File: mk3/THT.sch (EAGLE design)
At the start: 13 parts, among them IC1 74HC4053P

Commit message: Changed base resistor to 1k.
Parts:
- R3: value 330 -> 1K
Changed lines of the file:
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@@
 <grid distance="0.1" unitdist="inch" unit="inch" style="lines" multiple="1" display="no" altdistance="0.01" altunitdist="inch" altunit="inch"/>
 <layers>
-<layer number="1" name="Top" color="4" fill="1" visible="yes" active="no"/>
-<layer number="16" name="Bottom" color="1" fill="1" visible="yes" active="no"/>
-<layer number="17" name="Pads" color="2" fill="1" visible="yes" active="no"/>
-<layer number="18" name="Vias" color="2" fill="1" visible="yes" active="no"/>
-<layer number="19" name="Unrouted" color="6" fill="1" visible="yes" active="no"/>
-<layer number="20" name="Dimension" color="15" fill="1" visible="yes" active="no"/>
-<layer number="21" name="tPlace" color="7" fill="1" visible="yes" active="no"/>
-<layer number="22" name="bPlace" color="7" fill="1" visible="yes" active="no"/>
-<layer number="23" name="tOrigins" color="15" fill="1" visible="yes" active="no"/>
-<layer number="24" name="bOrigins" color="15" fill="1" visible="yes" active="no"/>
-<layer number="25" name="tNames" color="7" fill="1" visible="yes" active="no"/>
-<layer number="26" name="bNames" color="7" fill="1" visible="yes" active="no"/>
-<layer number="27" name="tValues" color="7" fill="1" visible="yes" active="no"/>
-<layer number="28" name="bValues" color="7" fill="1" visible="yes" active="no"/>
+<layer number="1" name="Top" color="4" fill="1" visible="no" active="no"/>
+<layer number="16" name="Bottom" color="1" fill="1" visible="no" active="no"/>
+<layer number="17" name="Pads" color="2" fill="1" visible="no" active="no"/>
+<layer number="18" name="Vias" color="2" fill="1" visible="no" active="no"/>
+<layer number="19" name="Unrouted" color="6" fill="1" visible="no" active="no"/>
+<layer number="20" name="Dimension" color="15" fill="1" visible="no" active="no"/>
+<layer number="21" name="tPlace" color="7" fill="1" visible="no" active="no"/>
+<layer number="22" name="bPlace" color="7" fill="1" visible="no" active="no"/>
+<layer number="23" name="tOrigins" color="15" fill="1" visible="no" active="no"/>
+<layer number="24" name="bOrigins" color="15" fill="1" visible="no" active="no"/>
+<layer number="25" name="tNames" color="7" fill="1" visible="no" active="no"/>
+<layer number="26" name="bNames" color="7" fill="1" visible="no" active="no"/>
+<layer number="27" name="tValues" color="7" fill="1" visible="no" active="no"/>
+<layer number="28" name="bValues" color="7" fill="1" visible="no" active="no"/>
 <layer number="29" name="tStop" color="7" fill="3" visible="no" active="no"/>
 <layer number="30" name="bStop" color="7" fill="6" visible="no" active="no"/>
@@
 <layer number="35" name="tGlue" color="7" fill="4" visible="no" active="no"/>
 <layer number="36" name="bGlue" color="7" fill="5" visible="no" active="no"/>
-<layer number="37" name="tTest" color="7" fill="1" visible="yes" active="no"/>
-<layer number="38" name="bTest" color="7" fill="1" visible="yes" active="no"/>
+<layer number="37" name="tTest" color="7" fill="1" visible="no" active="no"/>
+<layer number="38" name="bTest" color="7" fill="1" visible="no" active="no"/>
 <layer number="39" name="tKeepout" color="4" fill="11" visible="no" active="no"/>
 <layer number="40" name="bKeepout" color="1" fill="11" visible="no" active="no"/>
@@
 <layer number="44" name="Drills" color="7" fill="1" visible="no" active="no"/>
 <layer number="45" name="Holes" color="7" fill="1" visible="no" active="no"/>
-<layer number="46" name="Milling" color="3" fill="1" visible="yes" active="no"/>
-<layer number="47" name="Measures" color="7" fill="1" visible="yes" active="no"/>
-<layer number="48" name="Document" color="7" fill="1" visible="yes" active="no"/>
-<layer number="49" name="Reference" color="7" fill="1" visible="yes" active="no"/>
-<layer number="50" name="dxf" color="7" fill="1" visible="yes" active="no"/>
-<layer number="51" name="tDocu" color="7" fill="1" visible="yes" active="no"/>
-<layer number="52" name="bDocu" color="7" fill="1" visible="yes" active="no"/>
-<layer number="53" name="tGND_GNDA" color="7" fill="9" visible="yes" active="no"/>
-<layer number="54" name="bGND_GNDA" color="1" fill="9" visible="yes" active="no"/>
-<layer number="56" name="wert" color="7" fill="1" visible="yes" active="no"/>
-<layer number="57" name="tCAD" color="7" fill="1" visible="yes" active="no"/>
-<layer number="59" name="tCarbon" color="7" fill="1" visible="yes" active="no"/>
-<layer number="60" name="bCarbon" color="7" fill="1" visible="yes" active="no"/>
+<layer number="46" name="Milling" color="3" fill="1" visible="no" active="no"/>
+<layer number="47" name="Measures" color="7" fill="1" visible="no" active="no"/>
+<layer number="48" name="Document" color="7" fill="1" visible="no" active="no"/>
+<layer number="49" name="Reference" color="7" fill="1" visible="no" active="no"/>
+<layer number="50" name="dxf" color="7" fill="1" visible="no" active="no"/>
+<layer number="51" name="tDocu" color="7" fill="1" visible="no" active="no"/>
+<layer number="52" name="bDocu" color="7" fill="1" visible="no" active="no"/>
+<layer number="53" name="tGND_GNDA" color="7" fill="9" visible="no" active="no"/>
+<layer number="54" name="bGND_GNDA" color="1" fill="9" visible="no" active="no"/>
+<layer number="56" name="wert" color="7" fill="1" visible="no" active="no"/>
+<layer number="57" name="tCAD" color="7" fill="1" visible="no" active="no"/>
+<layer number="59" name="tCarbon" color="7" fill="1" visible="no" active="no"/>
+<layer number="60" name="bCarbon" color="7" fill="1" visible="no" active="no"/>
 <layer number="90" name="Modules" color="5" fill="1" visible="yes" active="yes"/>
 <layer number="91" name="Nets" color="2" fill="1" visible="yes" active="yes"/>
@@
 <part name="T1" library="transistor-neu-to92" deviceset="*-NPN-" device="TO92-EBC" technology="2N3904"/>
 <part name="P+2" library="supply1" deviceset="VCC" device=""/>
-<part name="R3" library="rcl" deviceset="R-EU_" device="0207/2V" value="330"/>
+<part name="R3" library="rcl" deviceset="R-EU_" device="0207/2V" value="1K"/>
 <part name="GND3" library="supply1" deviceset="GND" device=""/>
 <part name="JP2" library="jumper" deviceset="JP2E" device=""/>

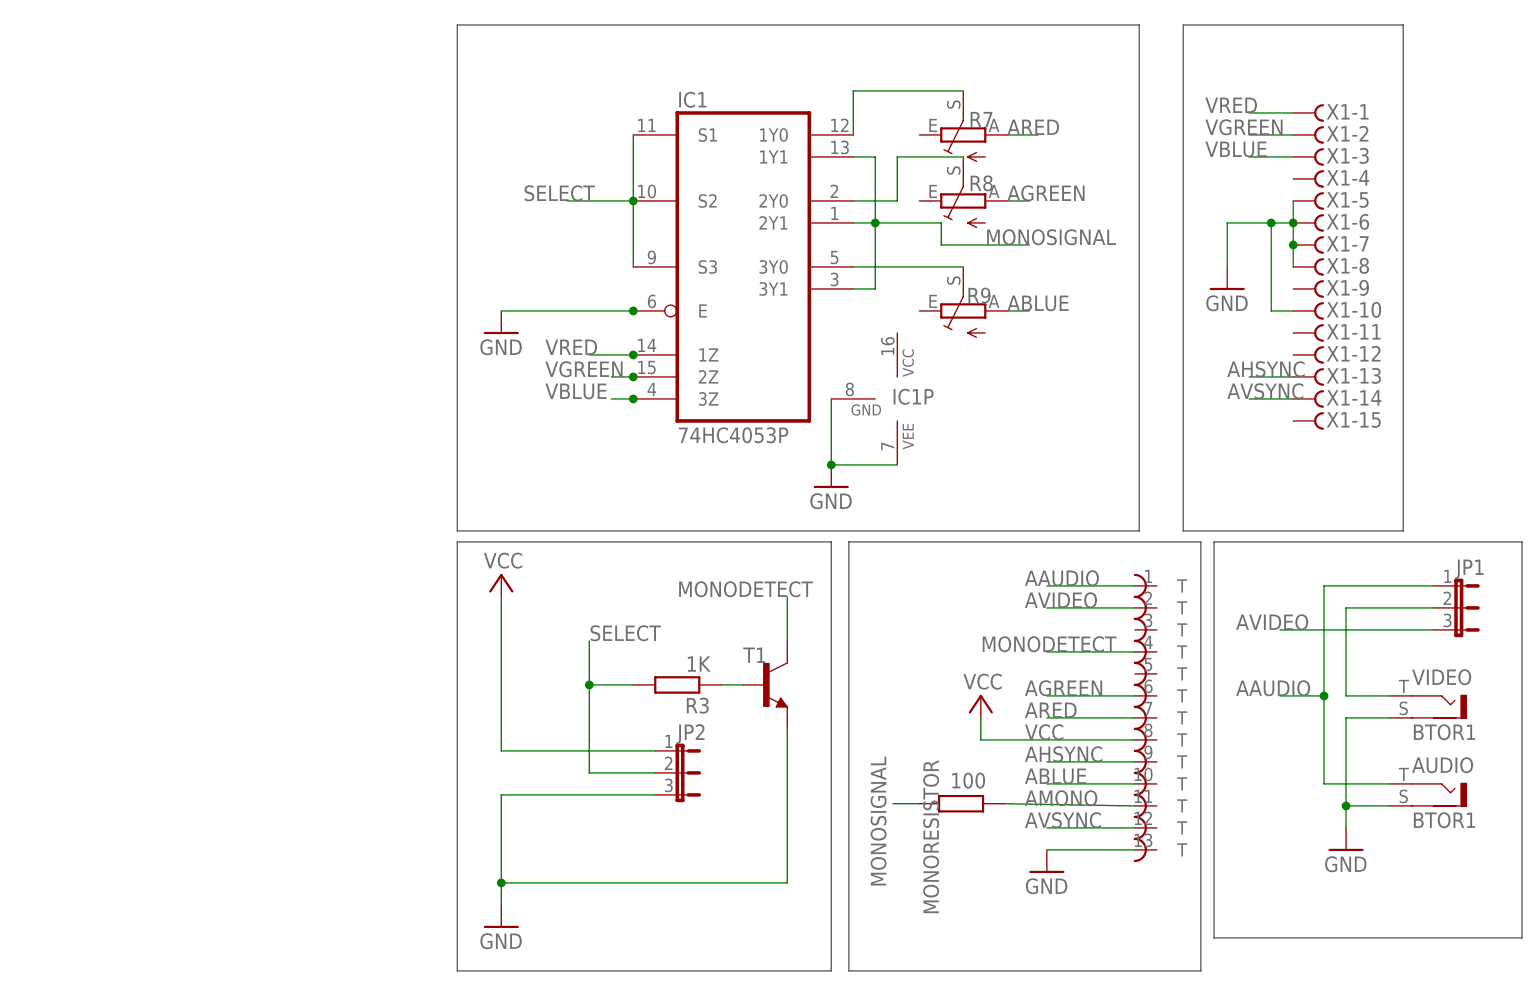
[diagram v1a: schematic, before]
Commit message: Switched to CD4053, didn't check the ratings on the HC-one.
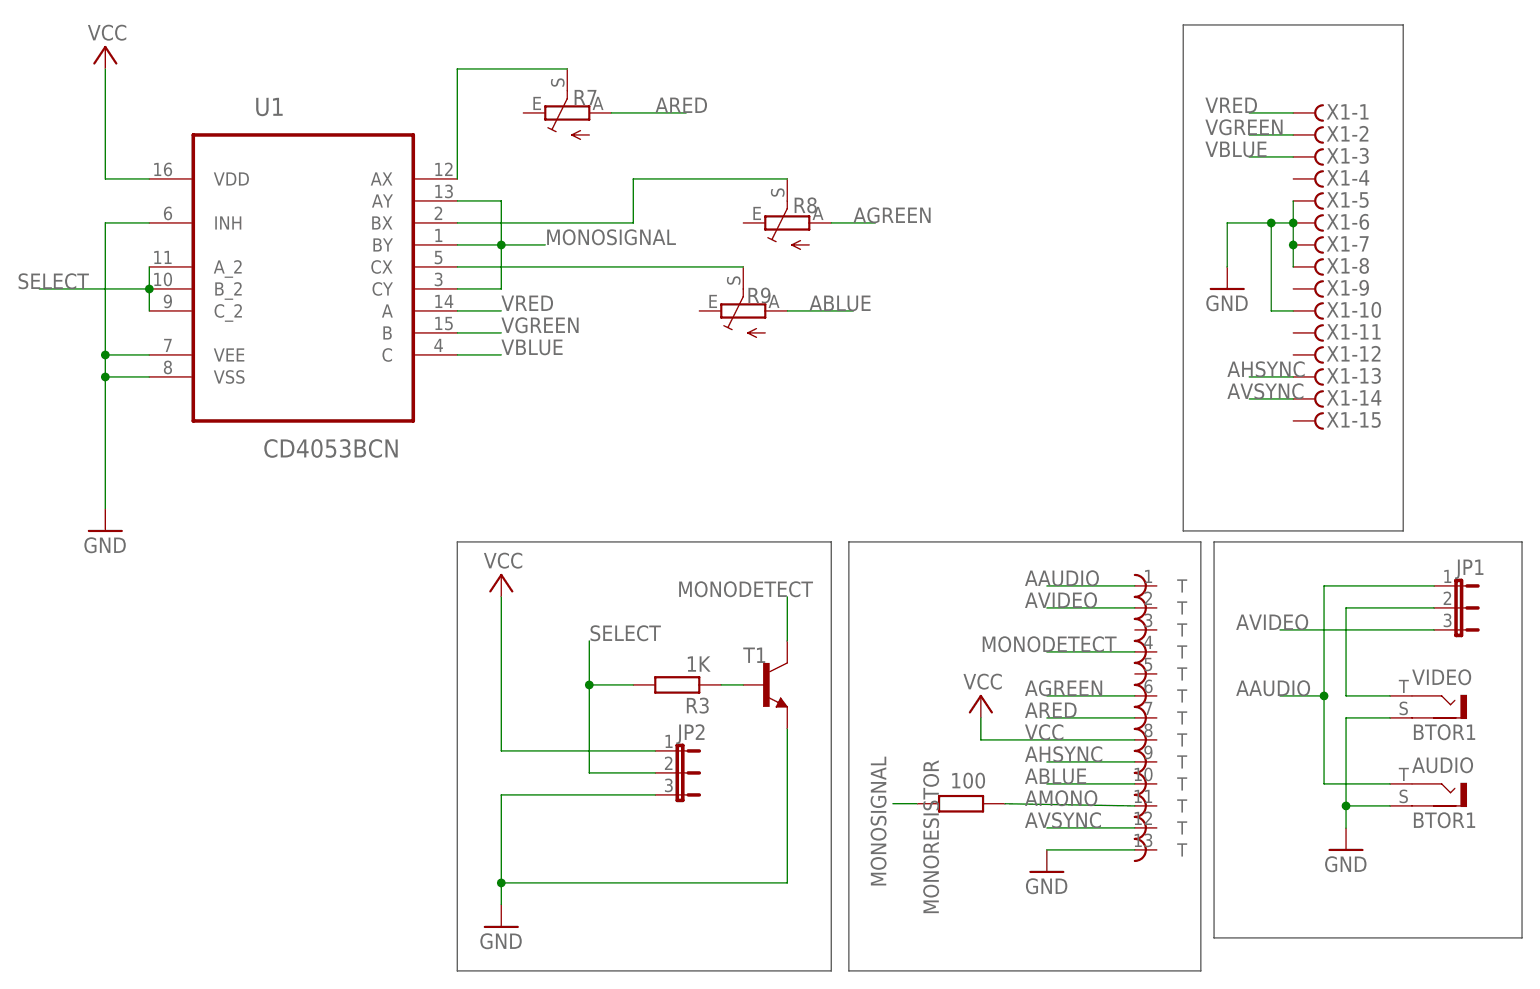
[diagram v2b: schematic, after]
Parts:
- removed IC1: 74HC4053P, 74xx-eu:74HC4053P
- added U1: CD4053BCN, Fairchild_By_element14_Batch_1:CD4053BCN
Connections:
- removed net N$4: IC1G$1.1Y0, R7.S
- removed net N$5: IC1G$1.2Y0, R8.S
- removed net N$6: IC1G$1.3Y0, R9.S
- new net N$1: R8.S, U1.BX
- new net N$2: R9.S, U1.CX
- new net N$9: R7.S, U1.AX
- net GND: now also U1.INH, U1.VEE, U1.VSS; no longer IC1G$1.E, IC1P.GND, IC1P.VEE
- net MONOSIGNAL: now also U1.AY, U1.BY, U1.CY; no longer IC1G$1.1Y1, IC1G$1.2Y1, IC1G$1.3Y1
- net SELECT: now also U1.A_2, U1.B_2, U1.C_2; no longer IC1G$1.S1, IC1G$1.S2, IC1G$1.S3
- net VBLUE: now also U1.C; no longer IC1G$1.3Z
- net VCC: now also U1.VDD
- net VGREEN: now also U1.B; no longer IC1G$1.2Z
- net VRED: now also U1.A; no longer IC1G$1.1Z
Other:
- moved on the sheet: R7, R8, R9
